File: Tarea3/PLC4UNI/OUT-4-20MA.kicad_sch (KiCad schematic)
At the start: 0 parts

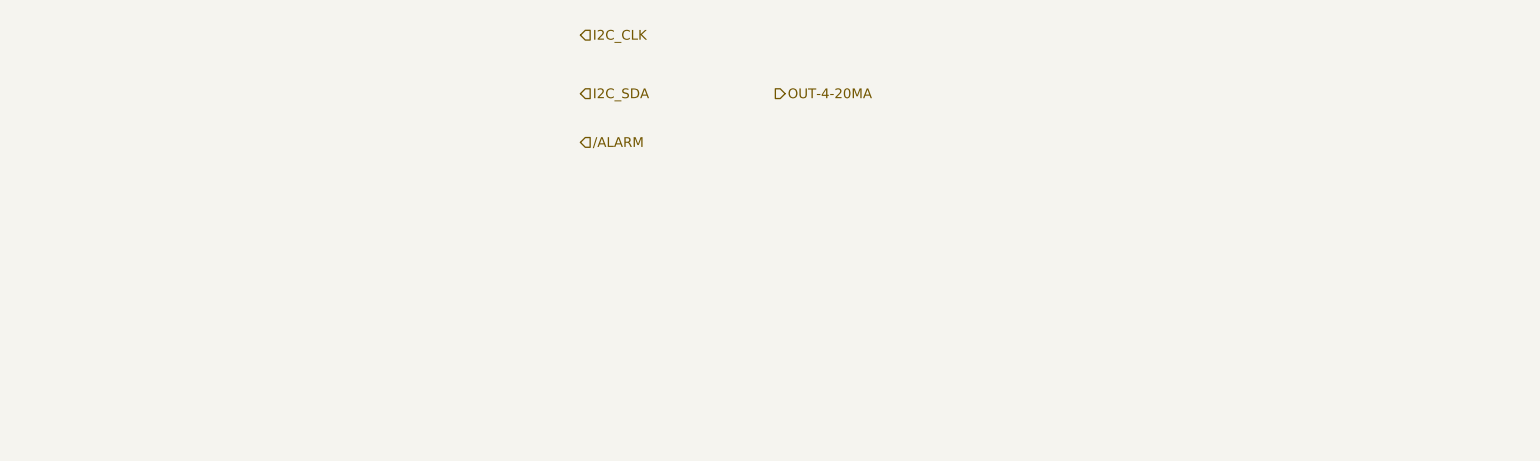
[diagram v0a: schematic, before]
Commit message: Cambio de directorio [Tarea2->CAD]
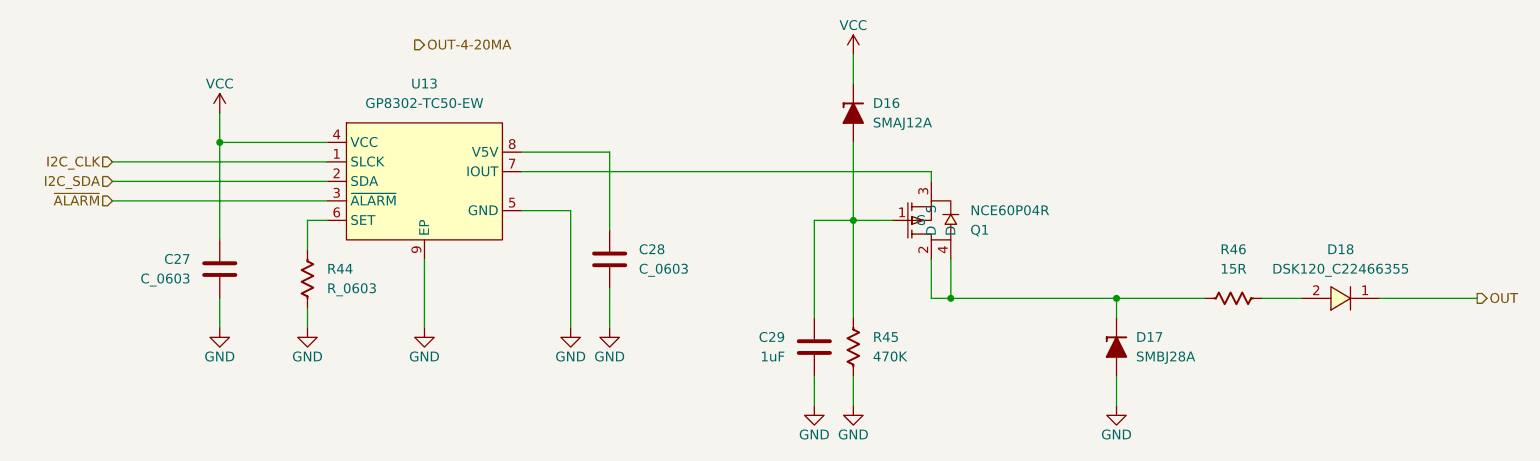
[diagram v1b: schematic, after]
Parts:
- added C27, C28: C_0603, PCM_Capacitor_SMD_AKL:C_0603_1608Metric, symbol PCM_Capacitor_US_AKL:C_0603
- added C29: 1uF, PCM_Capacitor_SMD_AKL:C_0603_1608Metric, symbol PCM_Capacitor_US_AKL:C_0603
- added D16: SMAJ12A, PCM_Diode_SMD_AKL:D_SMA, symbol PCM_Diode_TVS_AKL:SMAJ12A
- added D17: SMBJ28A, PCM_Diode_SMD_AKL:D_SMB, symbol PCM_Diode_TVS_AKL:SMBJ28A
- added D18: DSK120_C22466355, EasyEDA:SOD-123FL_L2.7-W1.8-LS3.8-RD, symbol EasyEDA:DSK120_C22466355
- added Q1: NCE60P04R, EasyEDA:SOT-223-3_L6.5-W3.4-P2.30-LS7.0-BR, symbol EasyEDA:NCE60P04R
- added R44: R_0603, PCM_Resistor_SMD_AKL:R_0603_1608Metric, symbol PCM_Resistor_US_AKL:R_0603
- added R45: 470K, PCM_Resistor_SMD_AKL:R_0603_1608Metric, symbol PCM_Resistor_US_AKL:R_0603
- added R46: 15R, PCM_Resistor_SMD_AKL:R_0805_2012Metric, symbol PCM_Resistor_US_AKL:R_0805
- added U13: GP8302-TC50-EW, EasyEDA:ESOP-8_L4.9-W3.9-P1.27-LS6.0-BL-EP, symbol EasyEDA:GP8302-TC50-EW
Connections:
- net I2C_CLK: now also U13.1 (SLCK)
- net I2C_SDA: now also U13.2 (SDA)
- new net: R44.1, U13.6 (SET)
- new net: D18.2, R46.1
- new net: D17.1 (K), Q1.2 (D), Q1.4 (D), R46.2
- new net: C29.1, D16.2 (A), Q1.1 (G), R45.1
- new net: Q1.3 (S), U13.7 (IOUT)
- new net: C28.1, U13.8 (V5V)
- new net GND: C27.2, C28.2, C29.2, D17.2 (A), R44.2, R45.2, U13.5 (GND), U13.9 (EP)
- new net OUT: D18.1
- new net VCC: C27.1, D16.1 (K), U13.4 (VCC)
- new net ~{ALARM}: U13.3 (~{ALARM})
